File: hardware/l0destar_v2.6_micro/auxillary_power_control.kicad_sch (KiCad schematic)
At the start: 6 parts

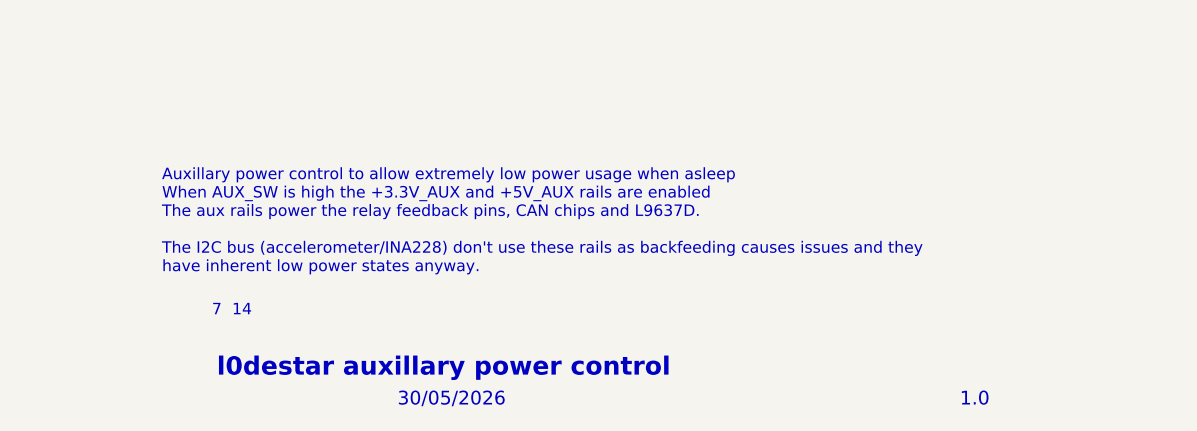
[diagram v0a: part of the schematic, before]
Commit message: update sheet annotations
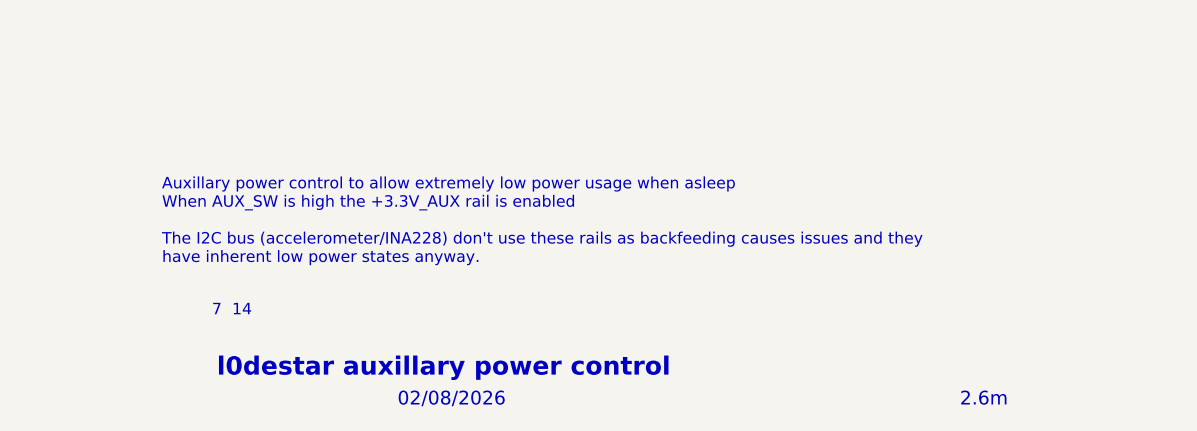
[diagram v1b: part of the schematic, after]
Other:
- note added: "02/08/2026"
- note added: "2.6m"
- note added: "Auxillary power control to allow extremely low power usage when asleep When AUX_SW is high the +3.3V_AUX rail is enabled The I2C bus (accelerometer/INA228) don't use these rails as backfeeding causes issues and they have inherent low power states anyway."
- note removed: "1.0"
- note removed: "30/05/2026"
- note removed: "Auxillary power control to allow extremely low power usage when asleep When AUX_SW is high the +3.3V_AUX and +5V_AUX rails are enabled The aux rails power the relay feedback pins, CAN chips and L9637D. The I2C bus (accelerometer/INA228) don't use these rails as backfeeding causes issues and they have inherent low power states anyway."
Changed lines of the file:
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@@
 	(generator_version "10.0")
 	(paper "A4")
-	(text "30/05/2026"
+	(text "02/08/2026"
 		(exclude_from_sim no)
 		(at 205.994 193.294 0)
@@
 		)
 	)
-	(text "Auxillary power control to allow extremely low power usage when asleep\nWhen AUX_SW is high the +3.3V_AUX and +5V_AUX rails are enabled\nThe aux rails power the relay feedback pins, CAN chips and L9637D.\n\nThe I2C bus (accelerometer/INA228) don't use these rails as backfeeding causes issues and they\nhave inherent low power states anyway."
+	(text "Auxillary power control to allow extremely low power usage when asleep\nWhen AUX_SW is high the +3.3V_AUX rail is enabled\n\nThe I2C bus (accelerometer/INA228) don't use these rails as backfeeding causes issues and they\nhave inherent low power states anyway."
 		(exclude_from_sim no)
 		(at 179.832 173.482 0)
@@
 		)
 	)
-	(text "1.0"
+	(text "2.6m"
 		(exclude_from_sim no)
 		(at 268.478 193.294 0)
